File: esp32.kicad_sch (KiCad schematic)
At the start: 25 parts, among them J12 DAT0, J13 DAT_DSP_1..8, J14 + -, J15 DAT_DSP_9..14, Q18 2N3904, Q19 2N3904, Q20 2N3904, U10 74LS241, U11 74LS241, U12 74LS241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

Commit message: schematic updated
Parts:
- removed Q18, Q19: 2N3904, Package_TO_SOT_THT:TO-92_Inline_Wide, symbol Transistor_BJT:2N3904
- removed R95, R96: 1k, Resistor_THT:R_Axial_DIN0207_L6.3mm_D2.5mm_P2.54mm_Vertical, symbol Device:R
- removed R97, R98: 10k, Resistor_THT:R_Axial_DIN0207_L6.3mm_D2.5mm_P2.54mm_Vertical, symbol Device:R
- removed U10, U11, U12, U15: 74LS241, Package_DIP:DIP-20_W7.62mm, symbol 74xx:74LS241
- added U10, U11, U12, U13: 74LS244, symbol 74xx:74LS244
- R90, R91: footprint Resistor_THT:R_Axial_DIN0207_L6.3mm_D2.5mm_P2.54mm_Vertical -> (none)
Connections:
- net +3.3V: now also R90.1, R91.1, U10.20 (VCC), U12.20 (VCC)
- net +5V: now also U11.20 (VCC), U13.20 (VCC)
- net DAT_DSP1: now also U10.2 (I0a), U11.18 (O0a)
- net DAT_DSP10: now also U12.4 (I1a), U13.16 (O1a)
- net DAT_DSP11: now also U12.6 (I2a), U13.14 (O2a)
- net DAT_DSP12: now also U12.8 (I3a), U13.12 (O3a)
- net DAT_DSP13: now also U12.11 (I0b), U13.9 (O0b)
- net DAT_DSP14: now also U12.13 (I1b), U13.7 (O1b)
- net DAT_DSP2: now also U10.4 (I1a), U11.16 (O1a)
- net DAT_DSP3: now also U10.6 (I2a), U11.14 (O2a)
- net DAT_DSP4: now also U10.8 (I3a), U11.12 (O3a)
- net DAT_DSP5: now also U10.11 (I0b), U11.9 (O0b)
- net DAT_DSP6: now also U10.13 (I1b), U11.7 (O1b)
- net DAT_DSP7: now also U10.15 (I2b), U11.5 (O2b)
- net DAT_DSP8: now also U10.17 (I3b), U11.3 (O3b)
- net DAT_DSP9: now also U12.2 (I0a), U13.18 (O0a)
- net DAT_ESP1: now also U10.18 (O0a), U11.2 (I0a)
- net DAT_ESP10: now also U12.16 (O1a), U13.4 (I1a)
- net DAT_ESP11: now also U12.14 (O2a), U13.6 (I2a)
- net DAT_ESP12: now also U12.12 (O3a), U13.8 (I3a)
- net DAT_ESP13: now also U12.9 (O0b), U13.11 (I0b)
- net DAT_ESP14: now also U12.7 (O1b), U13.13 (I1b)
- net DAT_ESP2: now also U10.16 (O1a), U11.4 (I1a)
- net DAT_ESP3: now also U10.14 (O2a), U11.6 (I2a)
- net DAT_ESP4: now also U10.12 (O3a), U11.8 (I3a)
- net DAT_ESP5: now also U10.9 (O0b), U11.11 (I0b)
- net DAT_ESP6: now also U9.19 (D2), U10.7 (O1b), U11.13 (I1b); no longer U9.18 (D15)
- net DAT_ESP7: now also U10.5 (O2b), U11.15 (I2b)
- net DAT_ESP8: now also U10.3 (O3b), U11.17 (I3b)
- net DAT_ESP9: now also U12.18 (O0a), U13.2 (I0a)
- net GND: now also U10.10 (GND), U11.10 (GND), U12.10 (GND), U12.15 (I2b), U12.17 (I3b), U12.3 (O3b), U12.5 (O2b), U13.10 (GND), U13.15 (I2b), U13.17 (I3b), U13.3 (O3b), U13.5 (O2b); no longer R90.2, R91.2
- removed net HIJACK: R90.1, U9.19 (D2)
- net LISTEN renamed ~{LISTEN}
- net ~{LISTEN}: now also R90.2, U10.1 (OEa), U10.19 (OEb), U12.1 (OEa), U12.19 (OEb); no longer R91.1
- new net ~{HIJACK}: R91.2, U11.1 (OEa), U11.19 (OEb), U13.1 (OEa), U13.19 (OEb), U9.18 (D15)

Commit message: assigned footprints
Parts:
- R90, R91: footprint (none) -> Resistor_THT:R_Axial_DIN0207_L6.3mm_D2.5mm_P2.54mm_Vertical
- U10, U11, U12, U13: footprint (none) -> Package_DIP:DIP-20_W7.62mm
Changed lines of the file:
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@@
       (effects (font (size 1.27 1.27)) (justify left))
     )
-    (property "Footprint" "" (id 2) (at 165.1 41.91 0)
+    (property "Footprint" "Package_DIP:DIP-20_W7.62mm" (id 2) (at 165.1 41.91 0)
       (effects (font (size 1.27 1.27)) hide)
     )
@@
       (effects (font (size 1.27 1.27)) (justify left))
     )
-    (property "Footprint" "" (id 2) (at 227.33 41.91 0)
+    (property "Footprint" "Package_DIP:DIP-20_W7.62mm" (id 2) (at 227.33 41.91 0)
       (effects (font (size 1.27 1.27)) hide)
     )
@@
       (effects (font (size 1.27 1.27)) (justify left))
     )
-    (property "Footprint" "" (id 2) (at 113.792 92.71 90)
+    (property "Footprint" "Resistor_THT:R_Axial_DIN0207_L6.3mm_D2.5mm_P2.54mm_Vertical" (id 2) (at 113.792 92.71 90)
       (effects (font (size 1.27 1.27)) hide)
     )
@@
       (effects (font (size 1.27 1.27)) (justify left))
     )
-    (property "Footprint" "" (id 2) (at 165.1 109.22 0)
+    (property "Footprint" "Package_DIP:DIP-20_W7.62mm" (id 2) (at 165.1 109.22 0)
       (effects (font (size 1.27 1.27)) hide)
     )
@@
       (effects (font (size 1.27 1.27)) (justify left))
     )
-    (property "Footprint" "" (id 2) (at 113.792 25.4 90)
+    (property "Footprint" "Resistor_THT:R_Axial_DIN0207_L6.3mm_D2.5mm_P2.54mm_Vertical" (id 2) (at 113.792 25.4 90)
       (effects (font (size 1.27 1.27)) hide)
     )
@@
       (effects (font (size 1.27 1.27)) (justify left))
     )
-    (property "Footprint" "" (id 2) (at 227.33 109.22 0)
-      (effects (font (size 1.27 1.27)) hide)
-    )
+    (property "Footprint" "Package_DIP:DIP-20_W7.62mm" (id 2) (at 227.33 109.22 0)
+      (effects (font (size 1.27 1.27)) hide)
+    )

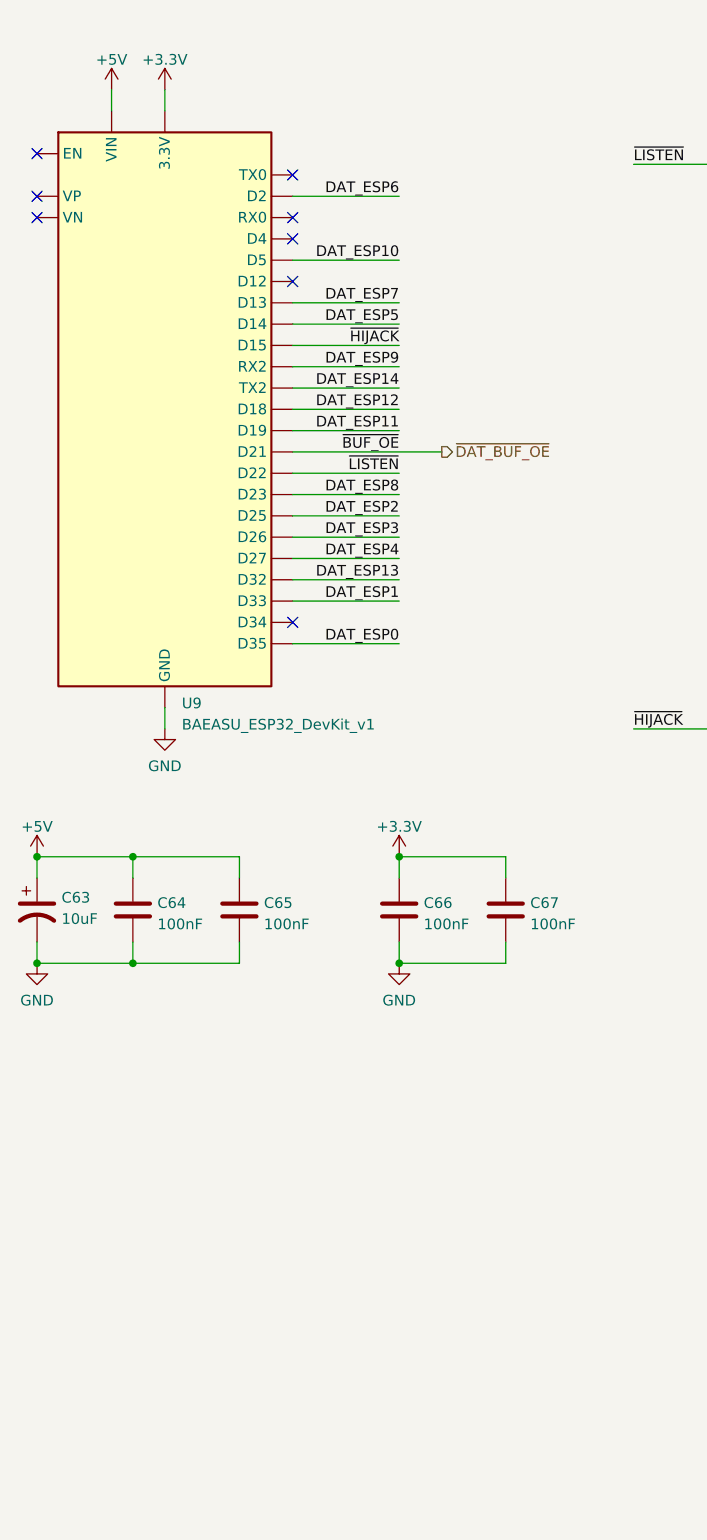
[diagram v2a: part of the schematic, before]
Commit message: add 3.3V 1A regulator
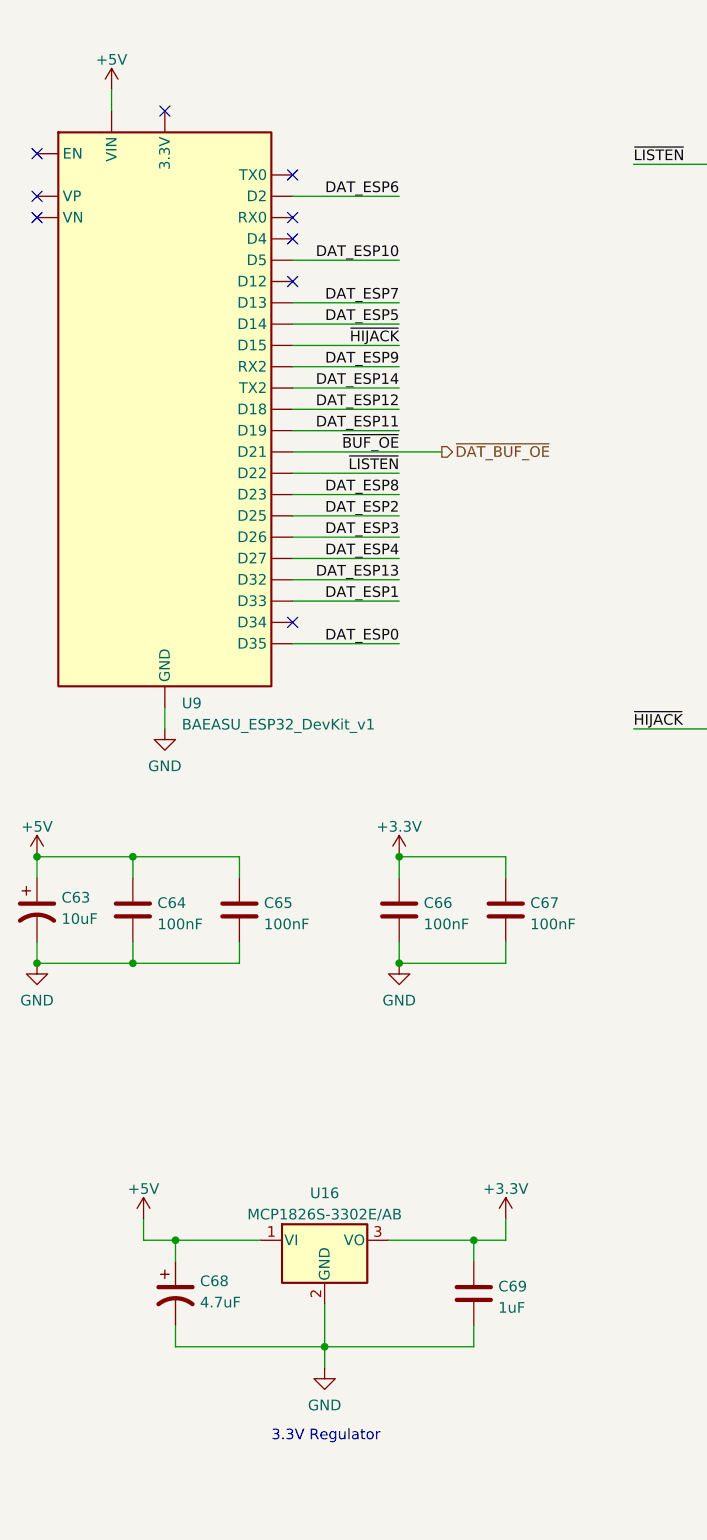
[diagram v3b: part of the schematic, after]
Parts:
- added C68: 4.7uF, Capacitor_THT:CP_Radial_D8.0mm_P5.00mm, symbol Device:C_Polarized_US
- added C69: 1uF, Capacitor_THT:C_Disc_D5.0mm_W2.5mm_P5.00mm, symbol Device:C
- added U16: MCP1826S-3302E/AB, Package_TO_SOT_THT:TO-220-3_Vertical, symbol Regulator_Linear:MCP1826S
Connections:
- net +3.3V: now also C69.1, U16.3 (VO); no longer U9.16 (3.3V)
- net +5V: now also C68.1, U16.1 (VI)
- net GND: now also C68.2, C69.2, U16.2 (GND)
- no-connect marks 8 -> 9
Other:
- note added: "3.3V Regulator"

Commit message: PCB rev 5
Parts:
- removed C63: 10uF, Capacitor_THT:C_Disc_D4.7mm_W2.5mm_P5.00mm, symbol Device:C_Polarized_US
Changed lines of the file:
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@@
   (junction (at 149.86 54.61) (diameter 0) (color 0 0 0 0)
   )
-  (junction (at 20.32 114.3) (diameter 0) (color 0 0 0 0)
-  )
   (junction (at 213.36 45.72) (diameter 0) (color 0 0 0 0)
   )
@@
   )
   (junction (at 63.5 114.3) (diameter 0) (color 0 0 0 0)
-  )
-  (junction (at 20.32 127) (diameter 0) (color 0 0 0 0)
   )
   (junction (at 135.89 173.99) (diameter 0) (color 0 0 0 0)
@@
     (stroke (width 0) (type default) (color 0 0 0 0))
   )
-  (wire (pts (xy 20.32 116.84) (xy 20.32 114.3))
-    (stroke (width 0) (type default) (color 0 0 0 0))
-  )
   (wire (pts (xy 203.2 109.22) (xy 214.63 109.22))
     (stroke (width 0) (type default) (color 0 0 0 0))
@@
     (stroke (width 0) (type default) (color 0 0 0 0))
   )
-  (wire (pts (xy 20.32 114.3) (xy 31.75 114.3))
-    (stroke (width 0) (type default) (color 0 0 0 0))
-  )
   (wire (pts (xy 140.97 101.6) (xy 152.4 101.6))
     (stroke (width 0) (type default) (color 0 0 0 0))
@@
     (stroke (width 0) (type default) (color 0 0 0 0))
   )
-  (wire (pts (xy 20.32 127) (xy 31.75 127))
-    (stroke (width 0) (type default) (color 0 0 0 0))
-  )
   (wire (pts (xy 140.97 96.52) (xy 152.4 96.52))
     (stroke (width 0) (type default) (color 0 0 0 0))
@@
   )
   (wire (pts (xy 72.39 170.18) (xy 72.39 172.72))
-    (stroke (width 0) (type default) (color 0 0 0 0))
-  )
-  (wire (pts (xy 20.32 124.46) (xy 20.32 127))
     (stroke (width 0) (type default) (color 0 0 0 0))
   )
@@
     (pin "1")
   )
-  (symbol (lib_id "power:+5V") (at 20.32 114.3 0) (unit 1)
-    (in_bom yes) (on_board yes) (fields_autoplaced)
-    (property "Reference" "#PWR03" (id 0) (at 20.32 118.11 0)
-      (effects (font (size 1.27 1.27)) hide)
-    )
-    (property "Value" "+5V" (id 1) (at 20.32 110.7242 0))
-    (property "Footprint" "" (id 2) (at 20.32 114.3 0)
-      (effects (font (size 1.27 1.27)) hide)
-    )
-    (property "Datasheet" "" (id 3) (at 20.32 114.3 0)
+  (symbol (lib_id "power:+5V") (at 31.75 114.3 0) (unit 1)
+    (in_bom yes) (on_board yes) (fields_autoplaced)
+    (property "Reference" "#PWR03" (id 0) (at 31.75 118.11 0)
+      (effects (font (size 1.27 1.27)) hide)
+    )
+    (property "Value" "+5V" (id 1) (at 31.75 110.7242 0))
+    (property "Footprint" "" (id 2) (at 31.75 114.3 0)
+      (effects (font (size 1.27 1.27)) hide)
+    )
+    (property "Datasheet" "" (id 3) (at 31.75 114.3 0)
       (effects (font (size 1.27 1.27)) hide)
     )
@@
     (pin "8")
     (pin "9")
-  )
-  (symbol (lib_id "Device:C_Polarized_US") (at 20.32 120.65 0) (unit 1)
-    (in_bom yes) (on_board yes) (fields_autoplaced)
-    (property "Reference" "C63" (id 0) (at 23.241 119.1803 0)
-      (effects (font (size 1.27 1.27)) (justify left))
-    )
-    (property "Value" "10uF" (id 1) (at 23.241 121.7172 0)
-      (effects (font (size 1.27 1.27)) (justify left))
-    )
-    (property "Footprint" "Capacitor_THT:C_Disc_D4.7mm_W2.5mm_P5.00mm" (id 2) (at 20.32 120.65 0)
-      (effects (font (size 1.27 1.27)) hide)
-    )
-    (property "Datasheet" "~" (id 3) (at 20.32 120.65 0)
-      (effects (font (size 1.27 1.27)) hide)
-    )
-    (pin "1")
-    (pin "2")
   )
   (symbol (lib_id "Connector_Generic:Conn_01x08") (at 245.11 132.08 0) (mirror y) (unit 1)
@@
     (pin "1")
   )
-  (symbol (lib_id "power:GND") (at 20.32 127 0) (unit 1)
-    (in_bom yes) (on_board yes) (fields_autoplaced)
-    (property "Reference" "#PWR04" (id 0) (at 20.32 133.35 0)
-      (effects (font (size 1.27 1.27)) hide)
-    )
-    (property "Value" "GND" (id 1) (at 20.32 131.4434 0))
-    (property "Footprint" "" (id 2) (at 20.32 127 0)
-      (effects (font (size 1.27 1.27)) hide)
-    )
-    (property "Datasheet" "" (id 3) (at 20.32 127 0)
-      (effects (font (size 1.27 1.27)) hide)
-    )
+  (symbol (lib_id "power:GND") (at 31.75 127 0) (unit 1)
+    (in_bom yes) (on_board yes) (fields_autoplaced)
+    (property "Reference" "#PWR04" (id 0) (at 31.75 133.35 0)
+      (effects (font (size 1.27 1.27)) hide)
+    )
+    (property "Value" "GND" (id 1) (at 31.75 131.4434 0))
+    (property "Footprint" "" (id 2) (at 31.75 127 0)
+      (effects (font (size 1.27 1.27)) hide)
+    )
+    (property "Datasheet" "" (id 3) (at 31.75 127 0)
+      (effects (font (size 1.27 1.27)) hide)
+    )

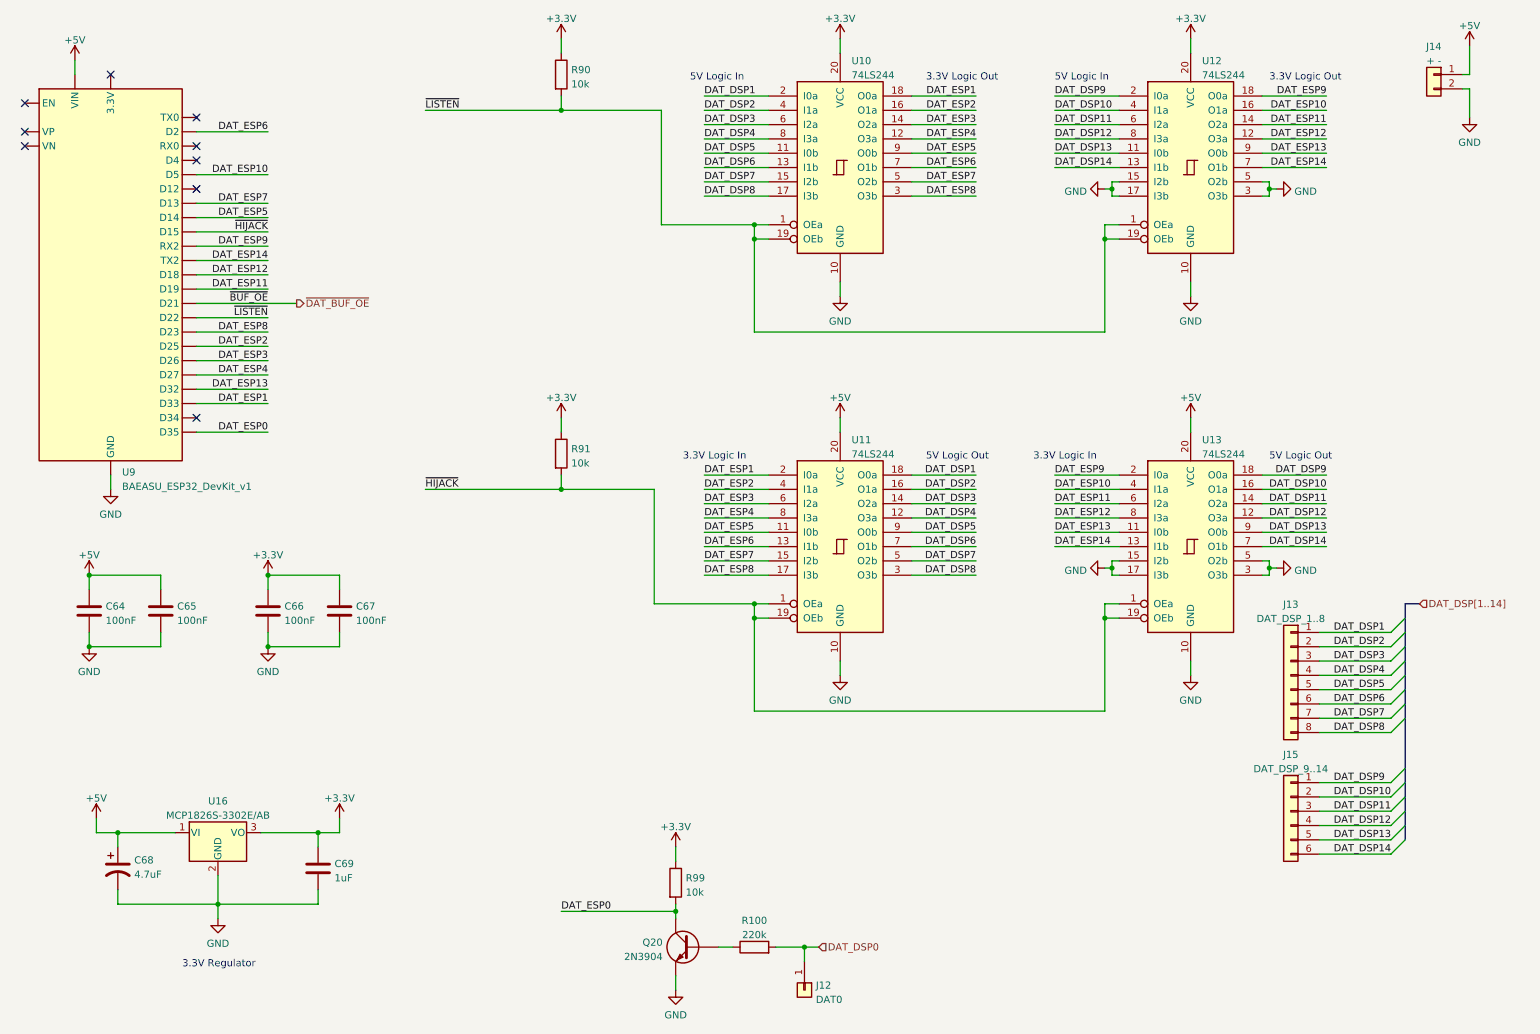
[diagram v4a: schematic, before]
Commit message: added vid_blk and fixed inverter on dat 0
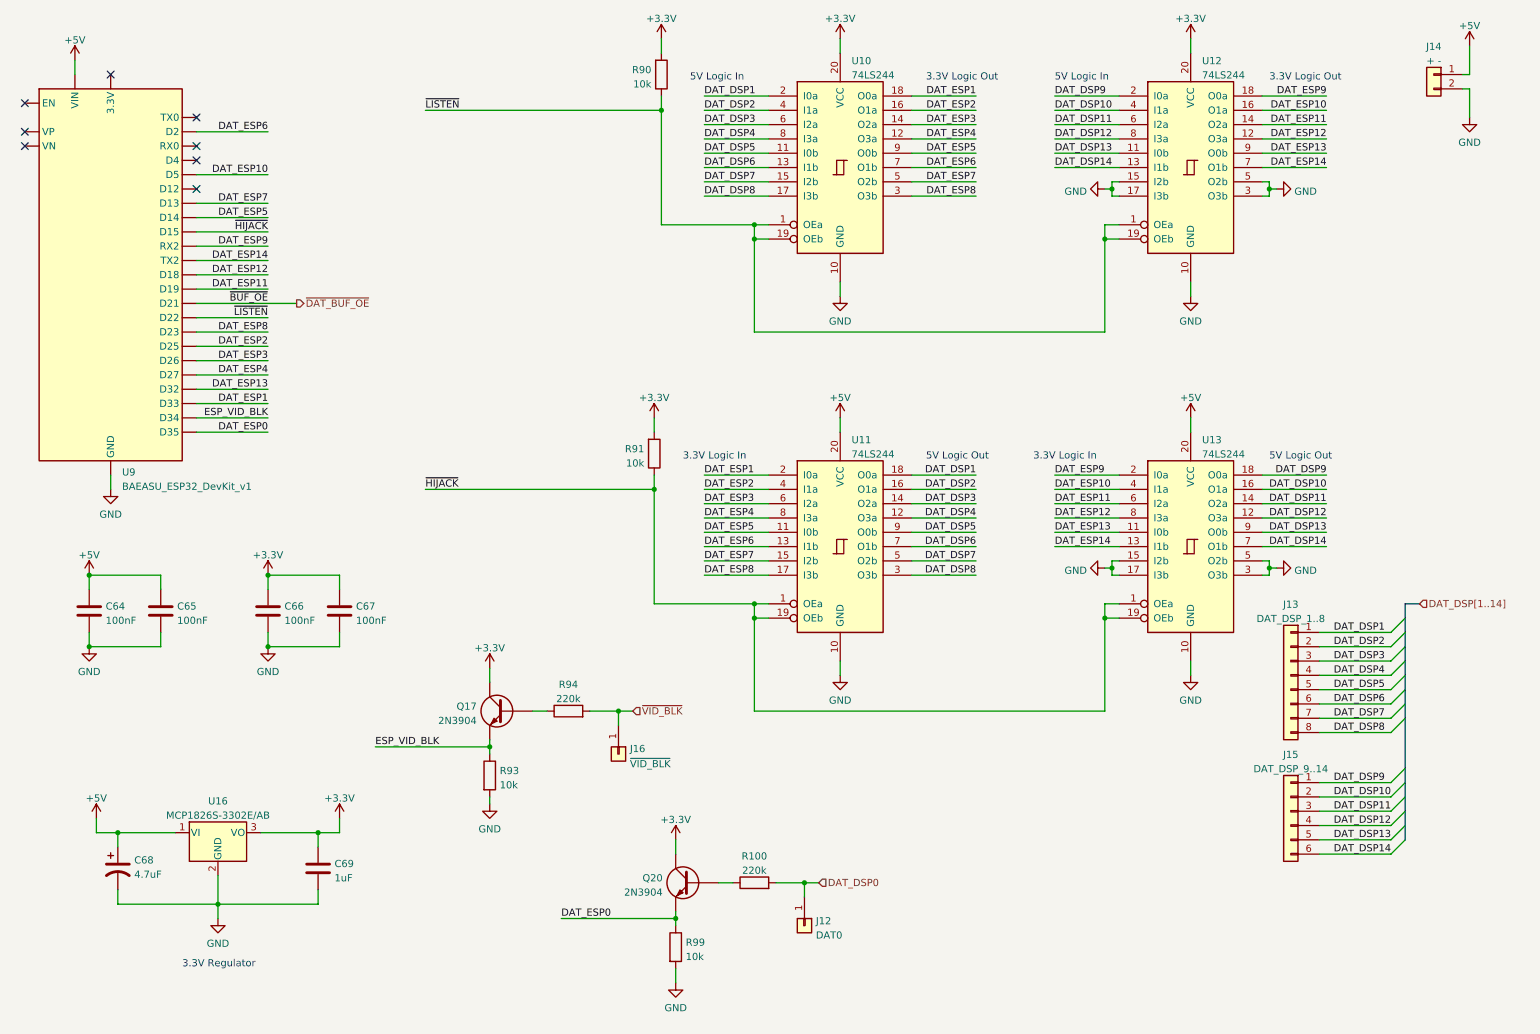
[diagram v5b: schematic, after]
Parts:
- added J16: ~{VID_BLK}, Connector_PinHeader_2.54mm:PinHeader_1x01_P2.54mm_Vertical, symbol Connector_Generic:Conn_01x01
- added Q17: 2N3904, Package_TO_SOT_THT:TO-92_Inline_Wide, symbol Transistor_BJT:2N3904
- added R93: 10k, Resistor_THT:R_Axial_DIN0207_L6.3mm_D2.5mm_P2.54mm_Vertical, symbol Device:R
- added R94: 220k, Resistor_THT:R_Axial_DIN0207_L6.3mm_D2.5mm_P2.54mm_Vertical, symbol Device:R
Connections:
- net +3.3V: now also Q20.3 (C), R90.2, R91.2, Q17.3 (C); no longer R90.1, R91.1, R99.1
- net DAT_ESP0: now also Q20.1 (E), R99.1; no longer Q20.3 (C), R99.2
- net GND: now also R99.2, R93.2; no longer Q20.1 (E)
- net ~{HIJACK}: now also R91.1; no longer R91.2
- net ~{LISTEN}: now also R90.1; no longer R90.2
- net ESP_VID_BLK: now reaches U9.4 (D34)
- net ESP_VID_BLK: now also Q17.1 (E), R93.1
- new net: Q17.2 (B), R94.1
- new net ~{VID_BLK}: J16.1 (Pin_1), R94.2
- no-connect marks 9 -> 8
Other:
- moved on the sheet: J12, Q20, R100, R90, R91, R99
